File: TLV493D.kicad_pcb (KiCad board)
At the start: 2 copper layers, 14 x 20 mm, 7 parts, among them J1 Conn_01x04_Female, U1 TLV493D

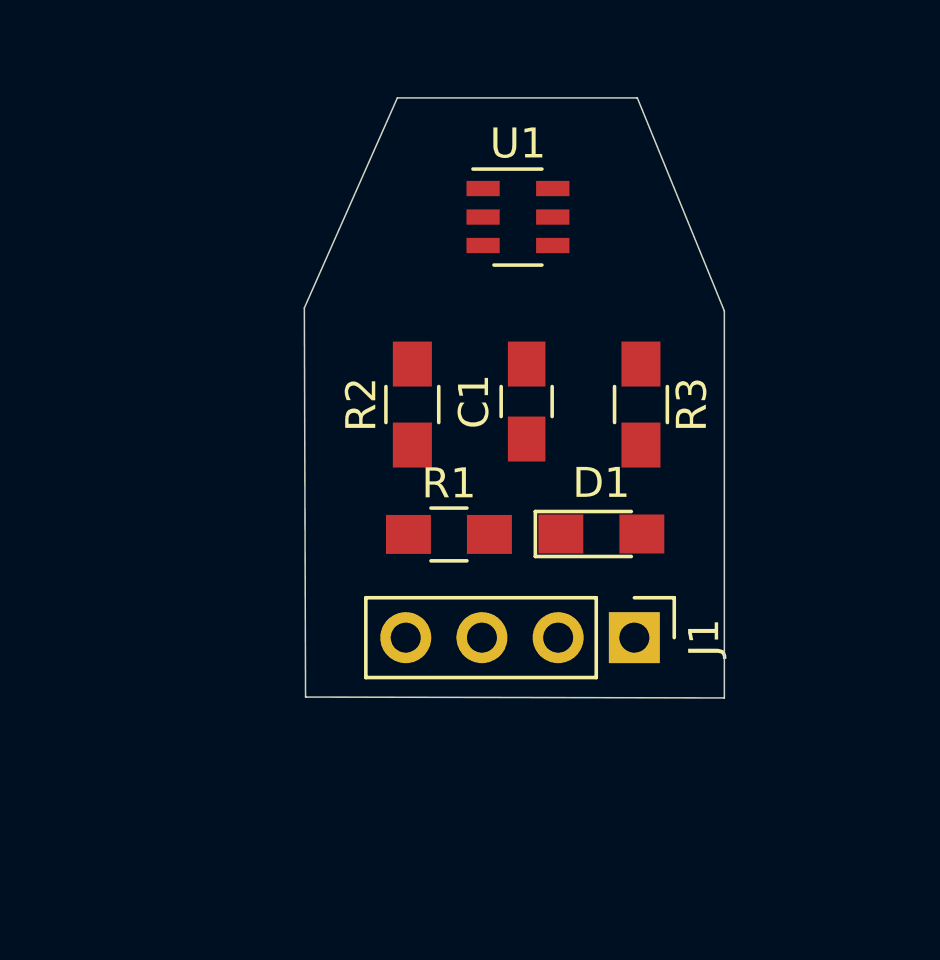
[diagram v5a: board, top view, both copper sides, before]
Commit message: fix contour
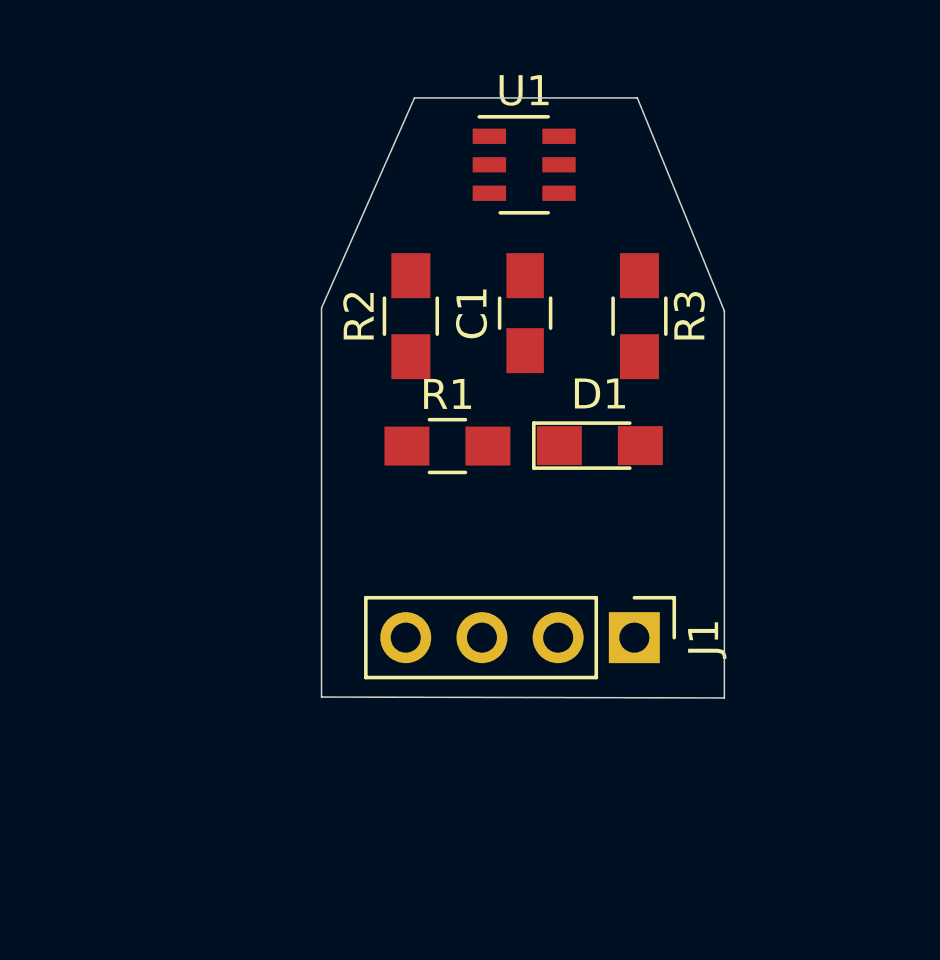
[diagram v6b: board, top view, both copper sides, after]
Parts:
- moved C1 2.95 mm to (154.3, 105.2)
- moved D1 2.95 mm to (156.7, 109.6)
- moved R1 2.95 mm to (151.7, 109.6)
- moved R2 2.95 mm to (150.4, 105.3)
- moved R3 2.95 mm to (158.1, 105.3)
- moved U1 1.75 mm to (154.2, 100.2)
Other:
- board size 14 x 20 mm -> 13.4 x 20 mm
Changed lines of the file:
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@@
-(kicad_pcb (version 20171130) (host pcbnew "(5.1.4-0-10_14)")
+(kicad_pcb (version 20171130) (host pcbnew "(5.1.4)-1")
   (general
     (thickness 1.6)
@@
     (35 F.Paste user)
     (36 B.SilkS user)
-    (37 F.SilkS user)
+    (37 F.SilkS user hide)
     (38 B.Mask user)
     (39 F.Mask user)
@@
   )
   (module Capacitors_SMD:C_0805_HandSoldering (layer F.Cu)
-    (at 154.31 108.12 90)
+    (at 154.2592 105.1736 90)
     (descr "Capacitor SMD 0805, hand soldering")
     (tags "capacitor 0805")
@@
   )
   (module LEDs:LED_0805_HandSoldering (layer F.Cu)
-    (at 156.8 112.535)
+    (at 156.7492 109.5886)
     (descr "Resistor SMD 0805, hand soldering")
     (tags "resistor 0805")
@@
   )
   (module Resistors_SMD:R_0805_HandSoldering (layer F.Cu)
-    (at 151.72 112.55)
+    (at 151.6692 109.6036)
     (descr "Resistor SMD 0805, hand soldering")
     (tags "resistor 0805")
@@
   )
   (module Resistors_SMD:R_0805_HandSoldering (layer F.Cu)
-    (at 150.5 108.22 90)
+    (at 150.4492 105.2736 90)
     (descr "Resistor SMD 0805, hand soldering")
     (tags "resistor 0805")
@@
   )
   (module Resistors_SMD:R_0805_HandSoldering (layer F.Cu)
-    (at 158.12 108.22 270)
+    (at 158.0692 105.2736 270)
     (descr "Resistor SMD 0805, hand soldering")
     (tags "resistor 0805")
@@
   )
   (module Housings_SSOP:TSOP-6_1.65x3.05mm_Pitch0.95mm (layer F.Cu)
-    (at 154.02 101.97)
+    (at 154.2288 100.2284)
     (descr "TSOP-6 package (comparable to TSOT-23), https://www.vishay.com/docs/71200/71200.pdf")
     (tags "Jedec MO-193C TSOP-6L")
@@
     )
   )
-  (gr_line (start 146.9 105) (end 146.94 117.97) (layer Edge.Cuts) (width 0.05))
-  (gr_line (start 146.94 117.97) (end 160.9 118) (layer Edge.Cuts) (width 0.05))
+  (gr_line (start 147.4724 105.0036) (end 150.5712 98) (layer Edge.Cuts) (width 0.05))
+  (gr_line (start 147.4724 117.97) (end 147.4724 105.0036) (layer Edge.Cuts) (width 0.05))
+  (gr_line (start 147.4724 117.97) (end 160.9 118) (layer Edge.Cuts) (width 0.05))
   (dimension 13.900176 (width 0.15) (layer Dwgs.User)
     (gr_text "13.900 mm" (at 153.993453 121.114984 -0.2885374576) (layer Dwgs.User)
@@
   )
   (dimension 13.90036 (width 0.15) (layer Dwgs.User)
-    (gr_text "13.900 mm" (at 154.01187 96.430053 -0.4121927414) (layer Dwgs.User)
-      (effects (font (size 1 1) (thickness 0.15)))
-    )
-    (feature1 (pts (xy 147 104.98) (xy 147.056737 97.093613)))
-    (feature2 (pts (xy 160.9 105.08) (xy 160.956737 97.193613)))
-    (crossbar (pts (xy 160.952518 97.780019) (xy 147.052518 97.680019)))
-    (arrow1a (pts (xy 147.052518 97.680019) (xy 148.183211 97.101718)))
-    (arrow1b (pts (xy 147.052518 97.680019) (xy 148.174774 98.274529)))
-    (arrow2a (pts (xy 160.952518 97.780019) (xy 159.830262 97.185509)))
-    (arrow2b (pts (xy 160.952518 97.780019) (xy 159.821825 98.35832)))
-  )
-  (gr_line (start 150 98) (end 146.9 105) (layer Edge.Cuts) (width 0.05))
+    (gr_text "13.900 mm" (at 154.01187 96.226853 -0.4121927414) (layer Dwgs.User)
+      (effects (font (size 1 1) (thickness 0.15)))
+    )
+    (feature1 (pts (xy 147 104.7768) (xy 147.056737 96.890413)))
+    (feature2 (pts (xy 160.9 104.8768) (xy 160.956737 96.990413)))
+    (crossbar (pts (xy 160.952518 97.576819) (xy 147.052518 97.476819)))
+    (arrow1a (pts (xy 147.052518 97.476819) (xy 148.183211 96.898518)))
+    (arrow1b (pts (xy 147.052518 97.476819) (xy 148.174774 98.071329)))
+    (arrow2a (pts (xy 160.952518 97.576819) (xy 159.830262 96.982309)))
+    (arrow2b (pts (xy 160.952518 97.576819) (xy 159.821825 98.15512)))
+  )
   (dimension 13.038405 (width 0.12) (layer F.SilkS)
     (gr_text "13.038 mm" (at 154.47889 104.609685 32.47119229) (layer F.SilkS)
@@
   (gr_line (start 160.9 105.1) (end 160.9 118) (layer Edge.Cuts) (width 0.05))
   (gr_line (start 158 98) (end 160.9 105.1) (layer Edge.Cuts) (width 0.05))
-  (gr_line (start 150 98) (end 158 98) (layer Edge.Cuts) (width 0.05))
+  (gr_line (start 150.5712 98) (end 158 98) (layer Edge.Cuts) (width 0.05))
 )

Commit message: update edge
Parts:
- moved U1 0.23 mm to (154.0, 100.2)
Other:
- outline, holes or cut-outs redrawn
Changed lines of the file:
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@@
-(kicad_pcb (version 20171130) (host pcbnew "(5.1.4)-1")
+(kicad_pcb (version 20171130) (host pcbnew "(5.1.4-0-10_14)")
   (general
     (thickness 1.6)
@@
   )
   (module Housings_SSOP:TSOP-6_1.65x3.05mm_Pitch0.95mm (layer F.Cu)
-    (at 154.2288 100.2284)
+    (at 154 100.22)
     (descr "TSOP-6 package (comparable to TSOT-23), https://www.vishay.com/docs/71200/71200.pdf")
     (tags "Jedec MO-193C TSOP-6L")
@@
     )
   )
-  (gr_line (start 147.4724 105.0036) (end 150.5712 98) (layer Edge.Cuts) (width 0.05))
-  (gr_line (start 147.4724 117.97) (end 147.4724 105.0036) (layer Edge.Cuts) (width 0.05))
+  (gr_line (start 147.4724 102.95) (end 152.02 97.99) (layer Edge.Cuts) (width 0.05))
+  (gr_line (start 147.4724 117.97) (end 147.4724 102.95) (layer Edge.Cuts) (width 0.05))
   (gr_line (start 147.4724 117.97) (end 160.9 118) (layer Edge.Cuts) (width 0.05))
   (dimension 13.900176 (width 0.15) (layer Dwgs.User)
@@
   )
   (dimension 13.90036 (width 0.15) (layer Dwgs.User)
-    (gr_text "13.900 mm" (at 154.01187 96.226853 -0.4121927414) (layer Dwgs.User)
-      (effects (font (size 1 1) (thickness 0.15)))
-    )
-    (feature1 (pts (xy 147 104.7768) (xy 147.056737 96.890413)))
-    (feature2 (pts (xy 160.9 104.8768) (xy 160.956737 96.990413)))
-    (crossbar (pts (xy 160.952518 97.576819) (xy 147.052518 97.476819)))
-    (arrow1a (pts (xy 147.052518 97.476819) (xy 148.183211 96.898518)))
-    (arrow1b (pts (xy 147.052518 97.476819) (xy 148.174774 98.071329)))
-    (arrow2a (pts (xy 160.952518 97.576819) (xy 159.830262 96.982309)))
-    (arrow2b (pts (xy 160.952518 97.576819) (xy 159.821825 98.15512)))
+    (gr_text "13.900 mm" (at 154.68187 96.230053 -0.4121927414) (layer Dwgs.User)
+      (effects (font (size 1 1) (thickness 0.15)))
+    )
+    (feature1 (pts (xy 147.67 104.78) (xy 147.726737 96.893613)))
+    (feature2 (pts (xy 161.57 104.88) (xy 161.626737 96.993613)))
+    (crossbar (pts (xy 161.622518 97.580019) (xy 147.722518 97.480019)))
+    (arrow1a (pts (xy 147.722518 97.480019) (xy 148.853211 96.901718)))
+    (arrow1b (pts (xy 147.722518 97.480019) (xy 148.844774 98.074529)))
+    (arrow2a (pts (xy 161.622518 97.580019) (xy 160.500262 96.985509)))
+    (arrow2b (pts (xy 161.622518 97.580019) (xy 160.491825 98.15832)))
   )
   (dimension 13.038405 (width 0.12) (layer F.SilkS)
@@
     (arrow2b (pts (xy 160.877763 105.134138) (xy 159.613779 105.010665)))
   )
-  (gr_line (start 160.9 105.1) (end 160.9 118) (layer Edge.Cuts) (width 0.05))
-  (gr_line (start 158 98) (end 160.9 105.1) (layer Edge.Cuts) (width 0.05))
-  (gr_line (start 150.5712 98) (end 158 98) (layer Edge.Cuts) (width 0.05))
+  (gr_line (start 160.89 102.99) (end 160.9 118) (layer Edge.Cuts) (width 0.05))
+  (gr_line (start 155.99 98) (end 160.89 102.99) (layer Edge.Cuts) (width 0.05))
+  (gr_line (start 152.02 97.99) (end 155.99 98) (layer Edge.Cuts) (width 0.05))
 )

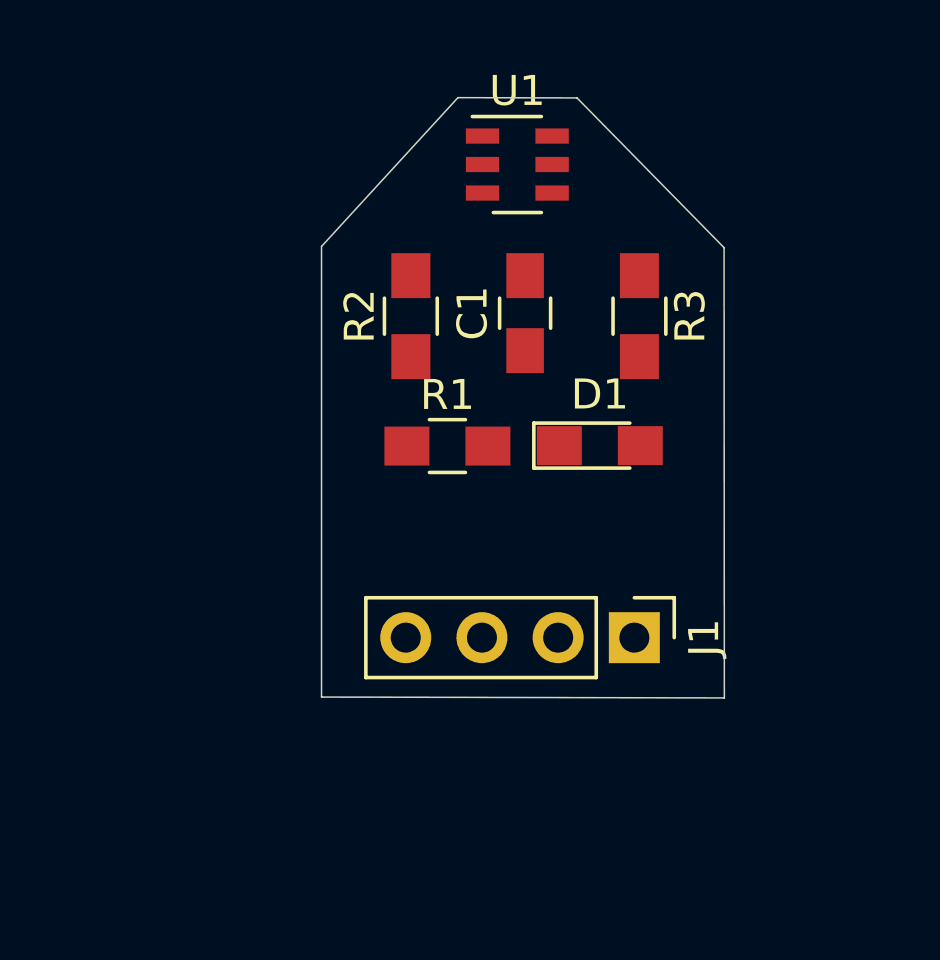
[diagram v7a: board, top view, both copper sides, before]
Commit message: update margin rect
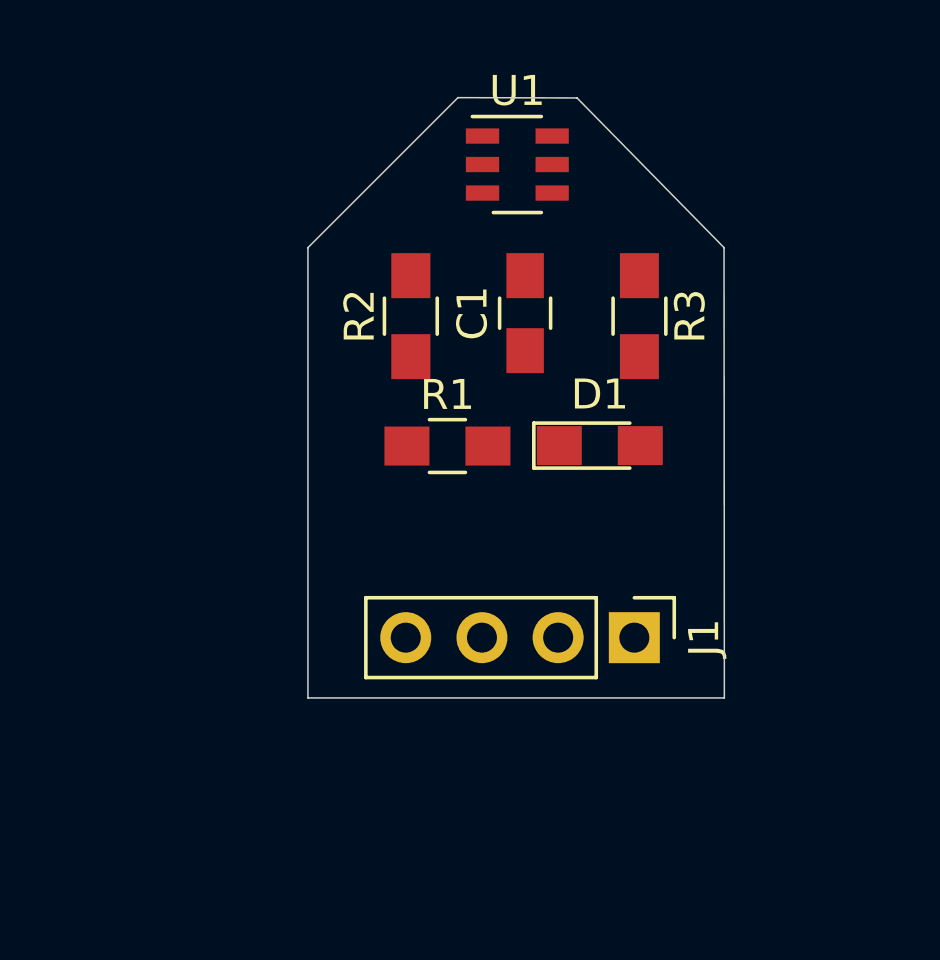
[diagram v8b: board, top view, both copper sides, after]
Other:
- board size 13.4 x 20 mm -> 13.9 x 20 mm
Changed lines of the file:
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@@
   (general
     (thickness 1.6)
-    (drawings 10)
+    (drawings 8)
     (tracks 0)
     (zones 0)
@@
     (35 F.Paste user)
     (36 B.SilkS user)
-    (37 F.SilkS user hide)
+    (37 F.SilkS user)
     (38 B.Mask user)
     (39 F.Mask user)
@@
     )
   )
-  (gr_line (start 147.4724 102.95) (end 152.02 97.99) (layer Edge.Cuts) (width 0.05))
-  (gr_line (start 147.4724 117.97) (end 147.4724 102.95) (layer Edge.Cuts) (width 0.05))
-  (gr_line (start 147.4724 117.97) (end 160.9 118) (layer Edge.Cuts) (width 0.05))
-  (dimension 13.900176 (width 0.15) (layer Dwgs.User)
-    (gr_text "13.900 mm" (at 153.993453 121.114984 -0.2885374576) (layer Dwgs.User)
+  (gr_line (start 147.02 102.99) (end 152.02 97.99) (layer Edge.Cuts) (width 0.05))
+  (gr_line (start 147.02 118) (end 147.02 102.99) (layer Edge.Cuts) (width 0.05))
+  (gr_line (start 147.02 118) (end 160.9 118) (layer Edge.Cuts) (width 0.05))
+  (dimension 13.900176 (width 0.15) (layer Margin)
+    (gr_text "13.900 mm" (at 153.993453 121.114984 -0.3) (layer Margin)
       (effects (font (size 1 1) (thickness 0.15)))
     )
@@
     (arrow2b (pts (xy 160.95 119.85) (xy 159.820557 120.43074)))
   )
-  (dimension 13.90036 (width 0.15) (layer Dwgs.User)
-    (gr_text "13.900 mm" (at 154.68187 96.230053 -0.4121927414) (layer Dwgs.User)
+  (dimension 13.90036 (width 0.15) (layer Margin)
+    (gr_text "13.900 mm" (at 154.68187 96.230053 -0.4) (layer Margin)
       (effects (font (size 1 1) (thickness 0.15)))
     )
@@
     (arrow2b (pts (xy 161.622518 97.580019) (xy 160.491825 98.15832)))
   )
-  (dimension 13.038405 (width 0.12) (layer F.SilkS)
-    (gr_text "13.038 mm" (at 154.47889 104.609685 32.47119229) (layer F.SilkS)
-      (effects (font (size 1 1) (thickness 0.15)))
-    )
-    (feature1 (pts (xy 147 105) (xy 148.611893 107.532975)))
-    (feature2 (pts (xy 158 98) (xy 159.611893 100.532975)))
-    (crossbar (pts (xy 159.297058 100.038235) (xy 148.297058 107.038235)))
-    (arrow1a (pts (xy 148.297058 107.038235) (xy 148.932611 105.938702)))
-    (arrow1b (pts (xy 148.297058 107.038235) (xy 149.562281 106.928183)))
-    (arrow2a (pts (xy 159.297058 100.038235) (xy 158.031835 100.148287)))
-    (arrow2b (pts (xy 159.297058 100.038235) (xy 158.661505 101.137768)))
-  )
-  (dimension 13.008459 (width 0.12) (layer F.SilkS)
-    (gr_text "13.008 mm" (at 154.734599 102.648292 -33.07926146) (layer F.SilkS)
-      (effects (font (size 1 1) (thickness 0.15)))
-    )
-    (feature1 (pts (xy 150 98) (xy 149.657695 98.52551)))
-    (feature2 (pts (xy 160.9 105.1) (xy 160.557695 105.62551)))
-    (crossbar (pts (xy 160.877763 105.134138) (xy 149.977763 98.034138)))
-    (arrow1a (pts (xy 149.977763 98.034138) (xy 151.241747 98.157611)))
-    (arrow1b (pts (xy 149.977763 98.034138) (xy 150.601611 99.140354)))
-    (arrow2a (pts (xy 160.877763 105.134138) (xy 160.253915 104.027922)))
-    (arrow2b (pts (xy 160.877763 105.134138) (xy 159.613779 105.010665)))
-  )
   (gr_line (start 160.89 102.99) (end 160.9 118) (layer Edge.Cuts) (width 0.05))
